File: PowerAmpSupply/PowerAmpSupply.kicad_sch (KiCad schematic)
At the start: 89 parts, among them J1 VIN_BRIDGE, J2 VIN_BRIDGE, J3 GND_BRIDGE, J4 GND_BRIDGE, J5 VIN, J6 VOUT, J7 VTRK_EXT, M1 12V 6Vstart <100mA, Q1 EPC2306, Q2 PNP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

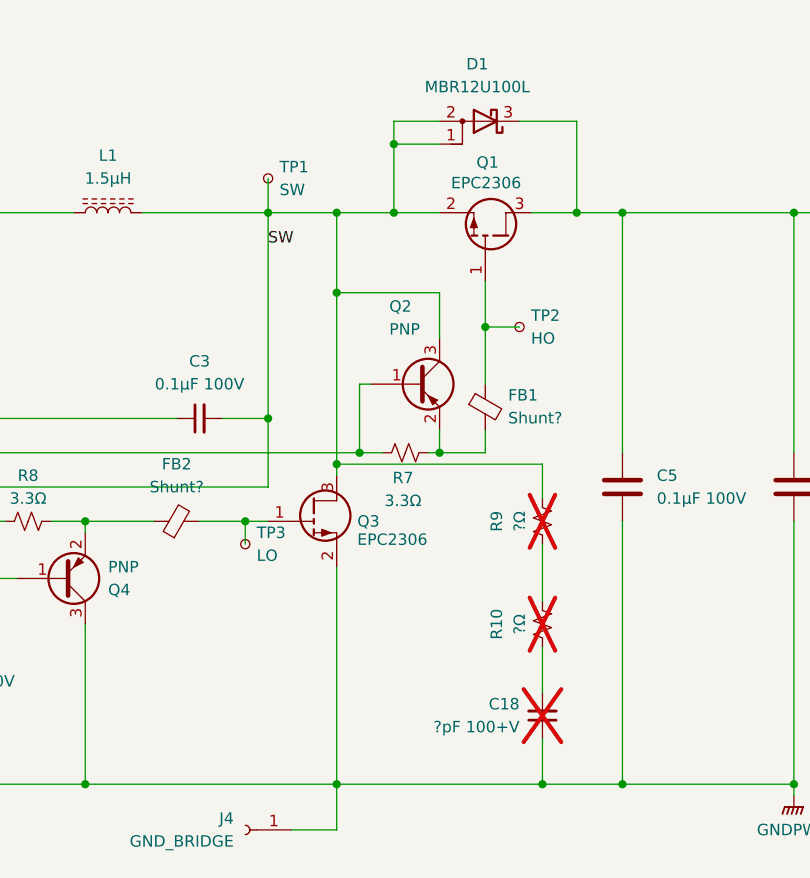
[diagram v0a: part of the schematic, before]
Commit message: PowerAmpSupply coax test connectors
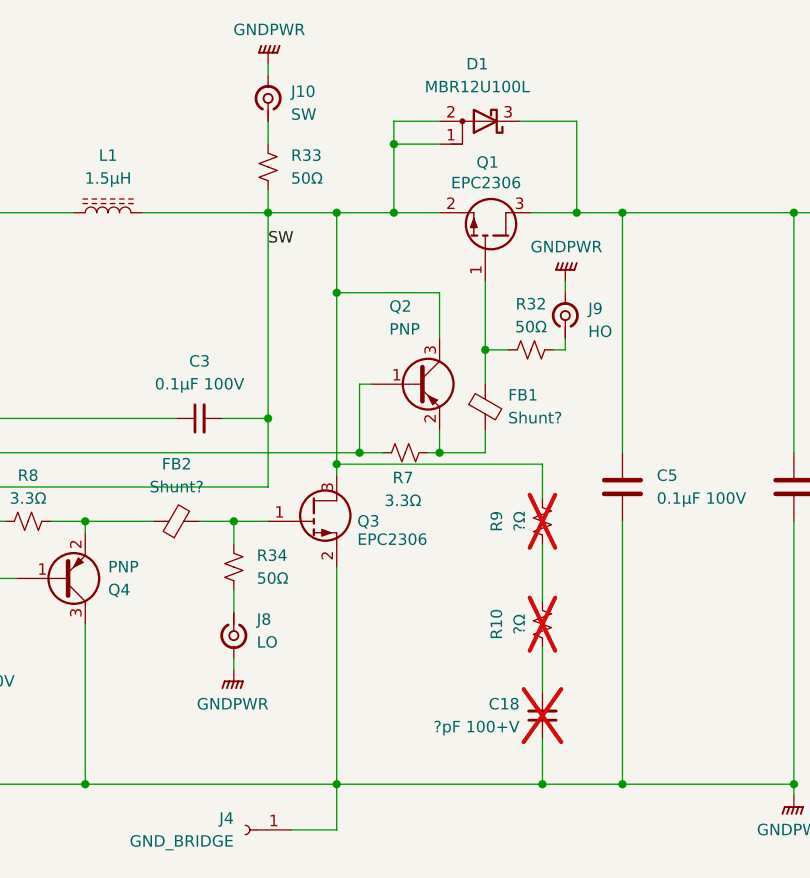
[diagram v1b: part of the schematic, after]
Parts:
- removed TP1: SW, TestPoint:TestPoint_Pad_D1.5mm, symbol Connector:TestPoint_Small
- removed TP2: HO, TestPoint:TestPoint_Pad_D1.5mm, symbol Connector:TestPoint_Small
- removed TP3: LO, TestPoint:TestPoint_Pad_D1.5mm, symbol Connector:TestPoint_Small
- added J10: SW, BW_Connectors:TE_CONMHF1-SMD, symbol Connector:Conn_Coaxial_Small
- added J8: LO, BW_Connectors:TE_CONMHF1-SMD, symbol Connector:Conn_Coaxial_Small
- added J9: HO, BW_Connectors:TE_CONMHF1-SMD, symbol Connector:Conn_Coaxial_Small
- added R32, R33, R34: 50Ω, Resistor_SMD:R_0402_1005Metric_Pad0.72x0.64mm_HandSolder, symbol Device:R_Small_US
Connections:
- net GND: now also J10.2 (Ext), J8.2 (Ext), J9.2 (Ext)
- net SW: now also R33.2
- net at FB1.1, Q1.1 (G): now also R32.1
- net at FB2.2, Q3.1 (G): now also R34.1
- new net: J10.1 (In), R33.1
- new net: J8.1 (In), R34.2
- new net: J9.1 (In), R32.2

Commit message: PowerAmpSupply VTRK change
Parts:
- R15: value 28kΩ 0.1% -> 84.5kΩ 0.1%; now fitted
- R16: value 28kΩ 0.1% -> 42.2kΩ 0.1%
- U2: now fitted
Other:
- note added: "Tracking voltage 0 - 3.3V VOUT = 10.873 * VTRK_EXT + 17.918V"
- note removed: "Tracking voltage 1.1V - 3.3V VOUT = 16.364 * VTRK_EXT"
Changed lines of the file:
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@@
 		)
 	)
-	(text "Tracking voltage\n1.1V - 3.3V\nVOUT = 16.364 * VTRK_EXT"
+	(text "Tracking voltage\n0 - 3.3V\nVOUT = 10.873 * VTRK_EXT + 17.918V"
 		(exclude_from_sim no)
 		(at 213.36 175.26 0)
@@
 		(in_bom yes)
 		(on_board yes)
-		(dnp yes)
+		(dnp no)
 		(fields_autoplaced yes)
 		(property "Reference" "R15"
@@
 			)
 		)
-		(property "Value" "28kΩ 0.1%"
+		(property "Value" "84.5kΩ 0.1%"
 			(at 198.12 193.0399 0)
 			(effects
@@
 		(in_bom yes)
 		(on_board yes)
-		(dnp yes)
+		(dnp no)
 		(fields_autoplaced yes)
 		(property "Reference" "U2"
@@
 			)
 		)
-		(property "Value" "28kΩ 0.1%"
+		(property "Value" "42.2kΩ 0.1%"
 			(at 215.9 193.0399 0)
 			(effects

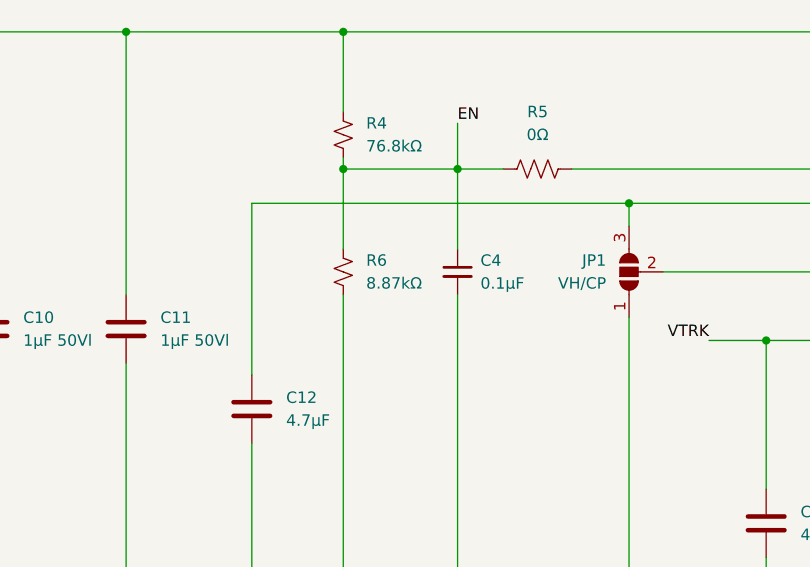
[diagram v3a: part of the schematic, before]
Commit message: PowerAmpSupply UVLO increase
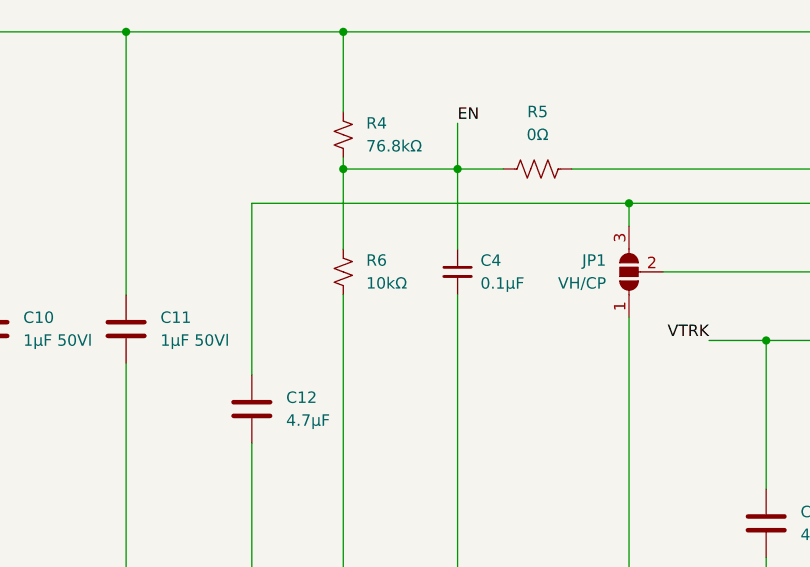
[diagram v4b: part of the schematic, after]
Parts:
- R6: value 8.87kΩ -> 10kΩ
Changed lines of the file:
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@@
 			)
 		)
-		(property "Value" "8.87kΩ"
+		(property "Value" "10kΩ"
 			(at 119.38 82.5499 0)
 			(effects

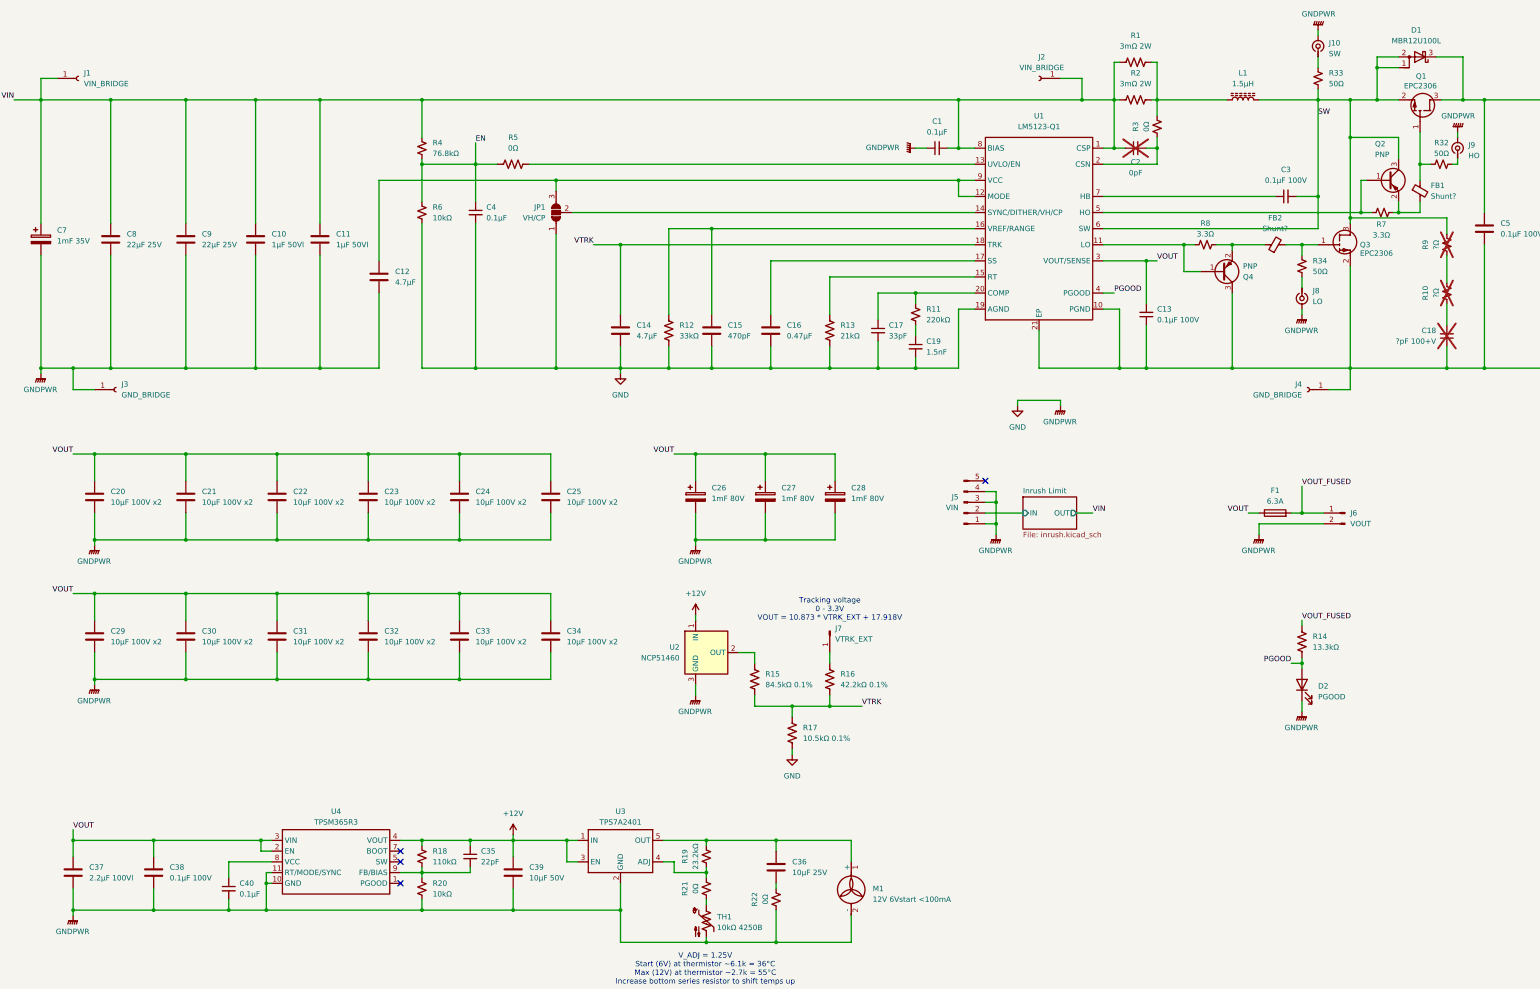
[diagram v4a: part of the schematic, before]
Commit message: PowerAmpSupply slower inrush applied and tested
Seems to work, so included the change in the design
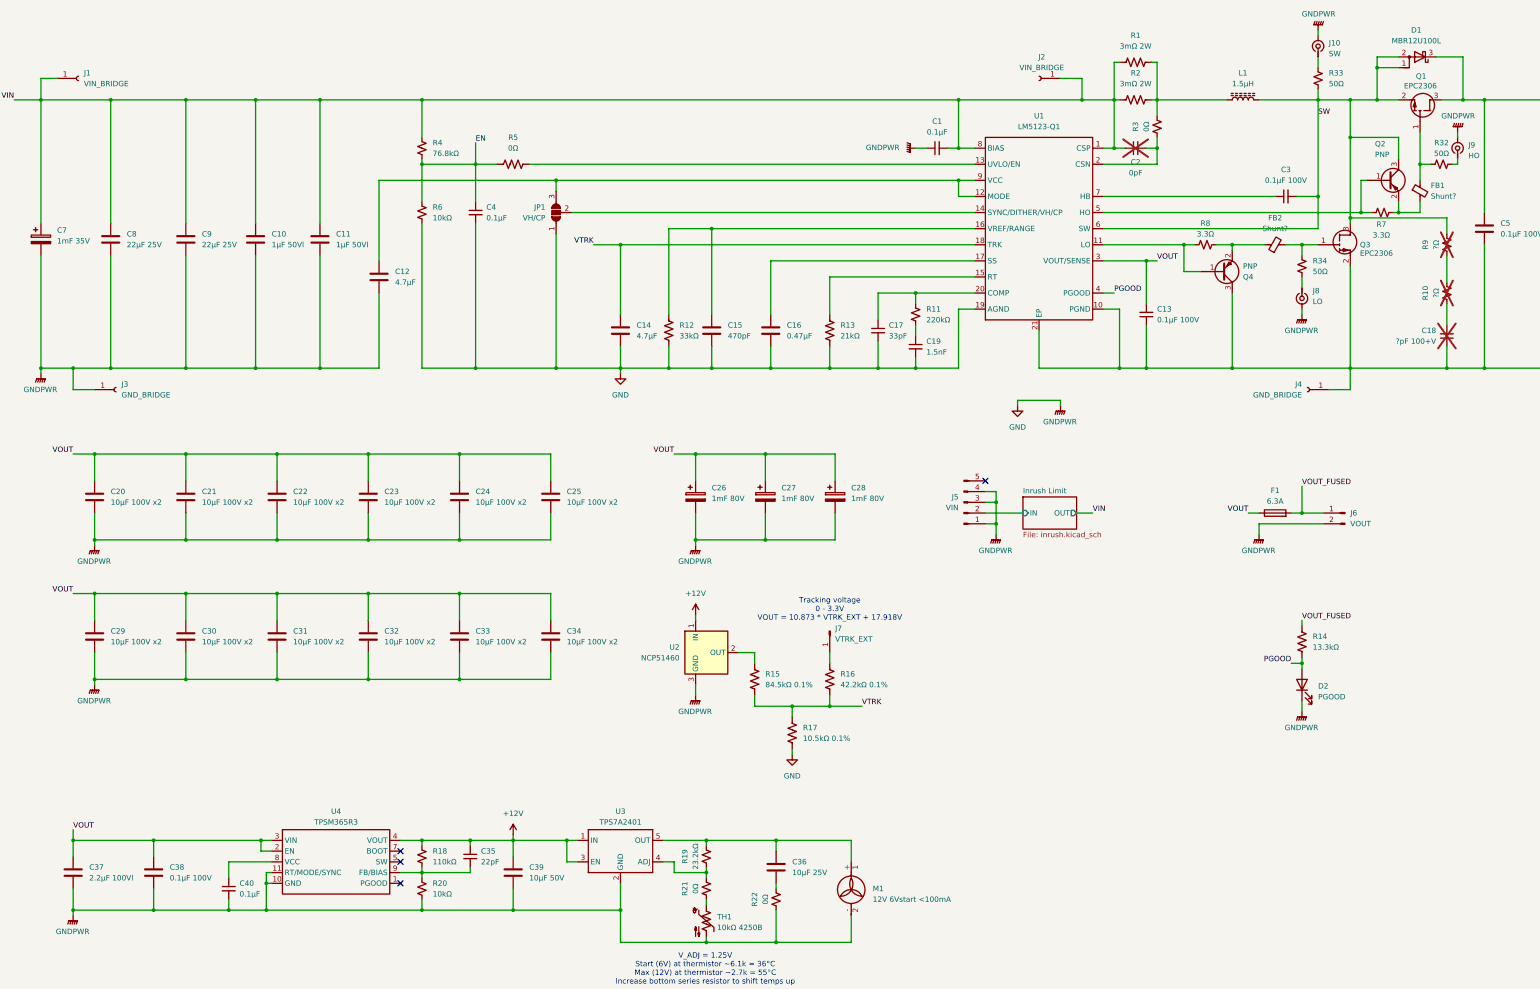
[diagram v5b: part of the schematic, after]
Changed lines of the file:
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@@
 (kicad_sch
-	(version 20231120)
+	(version 20250114)
 	(generator "eeschema")
-	(generator_version "8.0")
+	(generator_version "9.0")
 	(paper "A3")
+	(text "V_ADJ = 1.25V\nStart (6V) at thermistor ~6.1k = 36°C\nMax (12V) at thermistor ~2.7k = 55°C\nIncrease bottom series resistor to shift temps up"
+		(exclude_from_sim no)
+		(at 183.896 260.35 0)
+		(effects
+			(font
+				(size 1.27 1.27)
+			)
+		)
+	)
+	(text "Tracking voltage\n0 - 3.3V\nVOUT = 10.873 * VTRK_EXT + 17.918V"
+		(exclude_from_sim no)
+		(at 213.36 175.26 0)
+		(effects
+			(font
+				(size 1.27 1.27)
+			)
+		)
+	)
 	(junction
 		(at 184.15 229.87)
@@
 		)
 	)
-	(text "V_ADJ = 1.25V\nStart (6V) at thermistor ~6.1k = 36°C\nMax (12V) at thermistor ~2.7k = 55°C\nIncrease bottom series resistor to shift temps up"
-		(exclude_from_sim no)
-		(at 183.896 260.35 0)
-		(effects
-			(font
-				(size 1.27 1.27)
-			)
-		)
-	)
-	(text "Tracking voltage\n0 - 3.3V\nVOUT = 10.873 * VTRK_EXT + 17.918V"
-		(exclude_from_sim no)
-		(at 213.36 175.26 0)
-		(effects
-			(font
-				(size 1.27 1.27)
-			)
-		)
-	)
 	(label "PGOOD"
 		(at 280.67 100.33 0)
-		(fields_autoplaced yes)
 		(effects
 			(font
@@
 	(label "VIN"
 		(at 20.32 54.61 180)
-		(fields_autoplaced yes)
 		(effects
 			(font
@@
 	(label "VOUT"
 		(at 290.83 92.71 0)
-		(fields_autoplaced yes)
 		(effects
 			(font
@@
 	(label "VOUT_FUSED"
 		(at 325.12 177.8 0)
-		(fields_autoplaced yes)
 		(effects
 			(font
@@
 	(label "VOUT"
 		(at 34.29 171.45 180)
-		(fields_autoplaced yes)
 		(effects
 			(font
@@
 	(label "VOUT"
 		(at 34.29 138.43 180)
-		(fields_autoplaced yes)
 		(effects
 			(font
@@
 	(label "VIN"
 		(at 275.59 152.4 0)
-		(fields_autoplaced yes)
 		(effects
 			(font
@@
 	(label "VOUT"
 		(at 312.42 152.4 180)
-		(fields_autoplaced yes)
 		(effects
 			(font
@@
 	(label "VOUT"
 		(at 394.97 54.61 0)
-		(fields_autoplaced yes)
 		(effects
 			(font
@@
 	(label "VTRK"
 		(at 157.48 88.9 180)
-		(fields_autoplaced yes)
 		(effects
 			(font
@@
 	(label "VOUT"
 		(at 176.53 138.43 180)
-		(fields_autoplaced yes)
 		(effects
 			(font
@@
 	(label "PGOOD"
 		(at 322.58 187.96 180)
-		(fields_autoplaced yes)
 		(effects
 			(font
@@
 	(label "VOUT"
 		(at 34.29 227.33 0)
-		(fields_autoplaced yes)
 		(effects
 			(font
@@
 	(label "VTRK"
 		(at 220.98 198.12 0)
-		(fields_autoplaced yes)
 		(effects
 			(font
@@
 	(label "EN"
 		(at 129.54 64.77 0)
-		(fields_autoplaced yes)
 		(effects
 			(font
@@
 	(label "SW"
 		(at 328.93 58.42 0)
-		(fields_autoplaced yes)
 		(effects
 			(font
@@
 	(label "VOUT_FUSED"
 		(at 325.12 146.05 0)
-		(fields_autoplaced yes)
 		(effects
 			(font
@@
 		(at 259.08 148.59)
 		(size 12.7 7.62)
+		(exclude_from_sim no)
+		(in_bom yes)
+		(on_board yes)
+		(dnp no)
 		(fields_autoplaced yes)
 		(stroke
@@
 		)
 	)
+	(embedded_fonts no)
 )
